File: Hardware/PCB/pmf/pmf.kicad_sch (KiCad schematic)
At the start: 4 parts, among them J1 Conn_01x06_Pin, J2 Conn_01x05_Pin, J3 Conn_01x06_Socket, J4 Conn_01x05_Socket

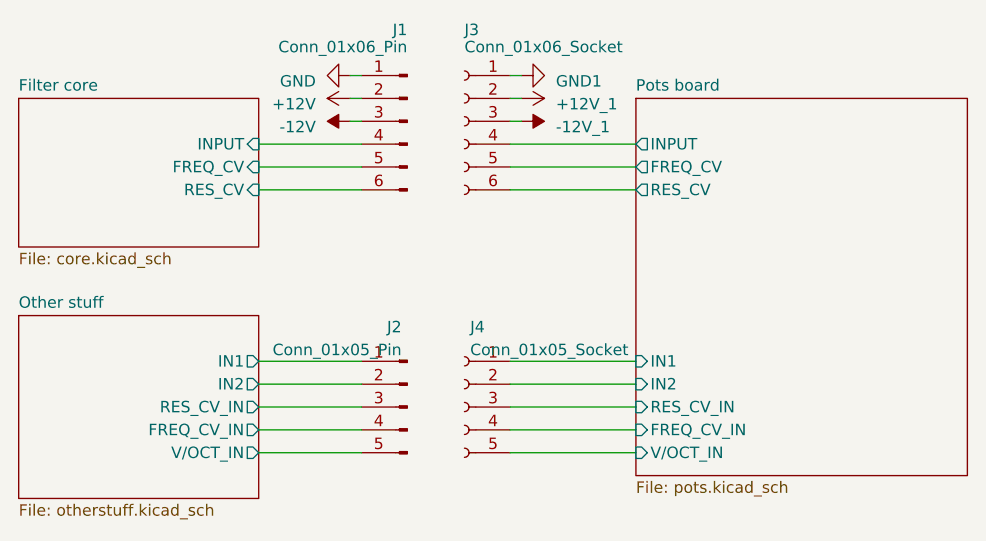
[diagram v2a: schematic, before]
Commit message: CVf test point; disambiguate heirarchical symbols
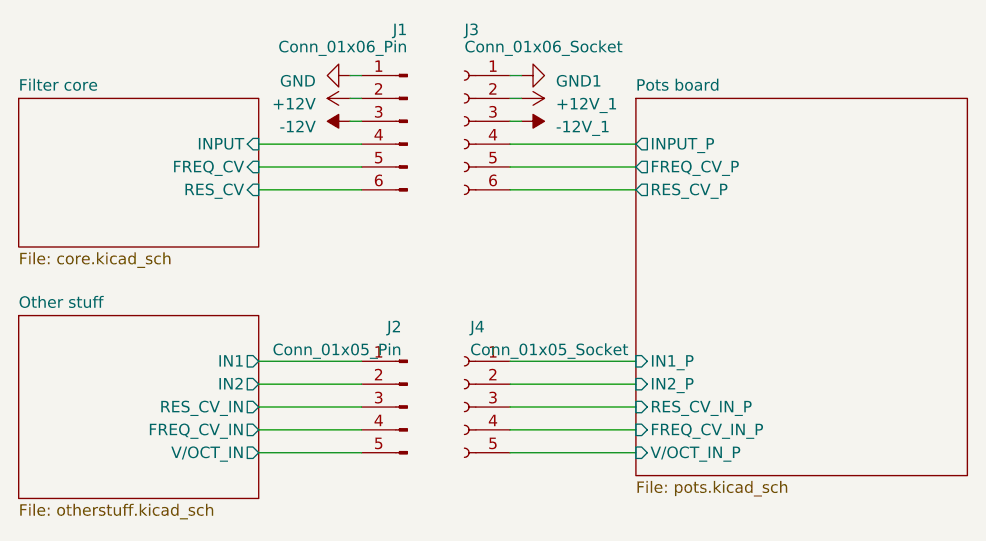
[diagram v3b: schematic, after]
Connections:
- net Pots board/FREQ_CV renamed Pots board/FREQ_CV_P
- net Pots board/FREQ_CV_IN renamed Pots board/FREQ_CV_IN_P
- net Pots board/IN1 renamed Pots board/IN1_P
- net Pots board/IN2 renamed Pots board/IN2_P
- net Pots board/INPUT renamed Pots board/INPUT_P
- net Pots board/RES_CV renamed Pots board/RES_CV_P
- net Pots board/RES_CV_IN renamed Pots board/RES_CV_IN_P
- net Pots board/V/OCT_IN renamed Pots board/V/OCT_IN_P
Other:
- sheet Pots board ports: added FREQ_CV_IN_P, FREQ_CV_P, IN1_P, IN2_P, INPUT_P, RES_CV_IN_P, RES_CV_P, V/OCT_IN_P; removed FREQ_CV, FREQ_CV_IN, IN1, IN2, INPUT, RES_CV, RES_CV_IN, V/OCT_IN
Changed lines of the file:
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@@
       (effects (font (size 1.27 1.27)) (justify left top))
     )
-    (pin "FREQ_CV" output (at 153.67 74.93 180)
+    (pin "FREQ_CV_P" output (at 153.67 74.93 180)
       (effects (font (size 1.27 1.27)) (justify left))
     )
-    (pin "RES_CV_IN" input (at 153.67 101.6 180)
+    (pin "RES_CV_IN_P" input (at 153.67 101.6 180)
       (effects (font (size 1.27 1.27)) (justify left))
     )
-    (pin "IN2" input (at 153.67 99.06 180)
+    (pin "IN2_P" input (at 153.67 99.06 180)
       (effects (font (size 1.27 1.27)) (justify left))
     )
-    (pin "INPUT" output (at 153.67 72.39 180)
+    (pin "INPUT_P" output (at 153.67 72.39 180)
       (effects (font (size 1.27 1.27)) (justify left))
     )
-    (pin "IN1" input (at 153.67 96.52 180)
+    (pin "IN1_P" input (at 153.67 96.52 180)
       (effects (font (size 1.27 1.27)) (justify left))
     )
-    (pin "V{slash}OCT_IN" input (at 153.67 106.68 180)
+    (pin "V{slash}OCT_IN_P" input (at 153.67 106.68 180)
       (effects (font (size 1.27 1.27)) (justify left))
     )
-    (pin "FREQ_CV_IN" input (at 153.67 104.14 180)
+    (pin "FREQ_CV_IN_P" input (at 153.67 104.14 180)
       (effects (font (size 1.27 1.27)) (justify left))
     )
-    (pin "RES_CV" output (at 153.67 77.47 180)
+    (pin "RES_CV_P" output (at 153.67 77.47 180)
       (effects (font (size 1.27 1.27)) (justify left))
     )
